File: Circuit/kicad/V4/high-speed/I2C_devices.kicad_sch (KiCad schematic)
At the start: 78 parts, among them U15 LSF0108PWR, U16 TCA9548APWR, U17 LSF0108PWR, U18 TCA9548APWR

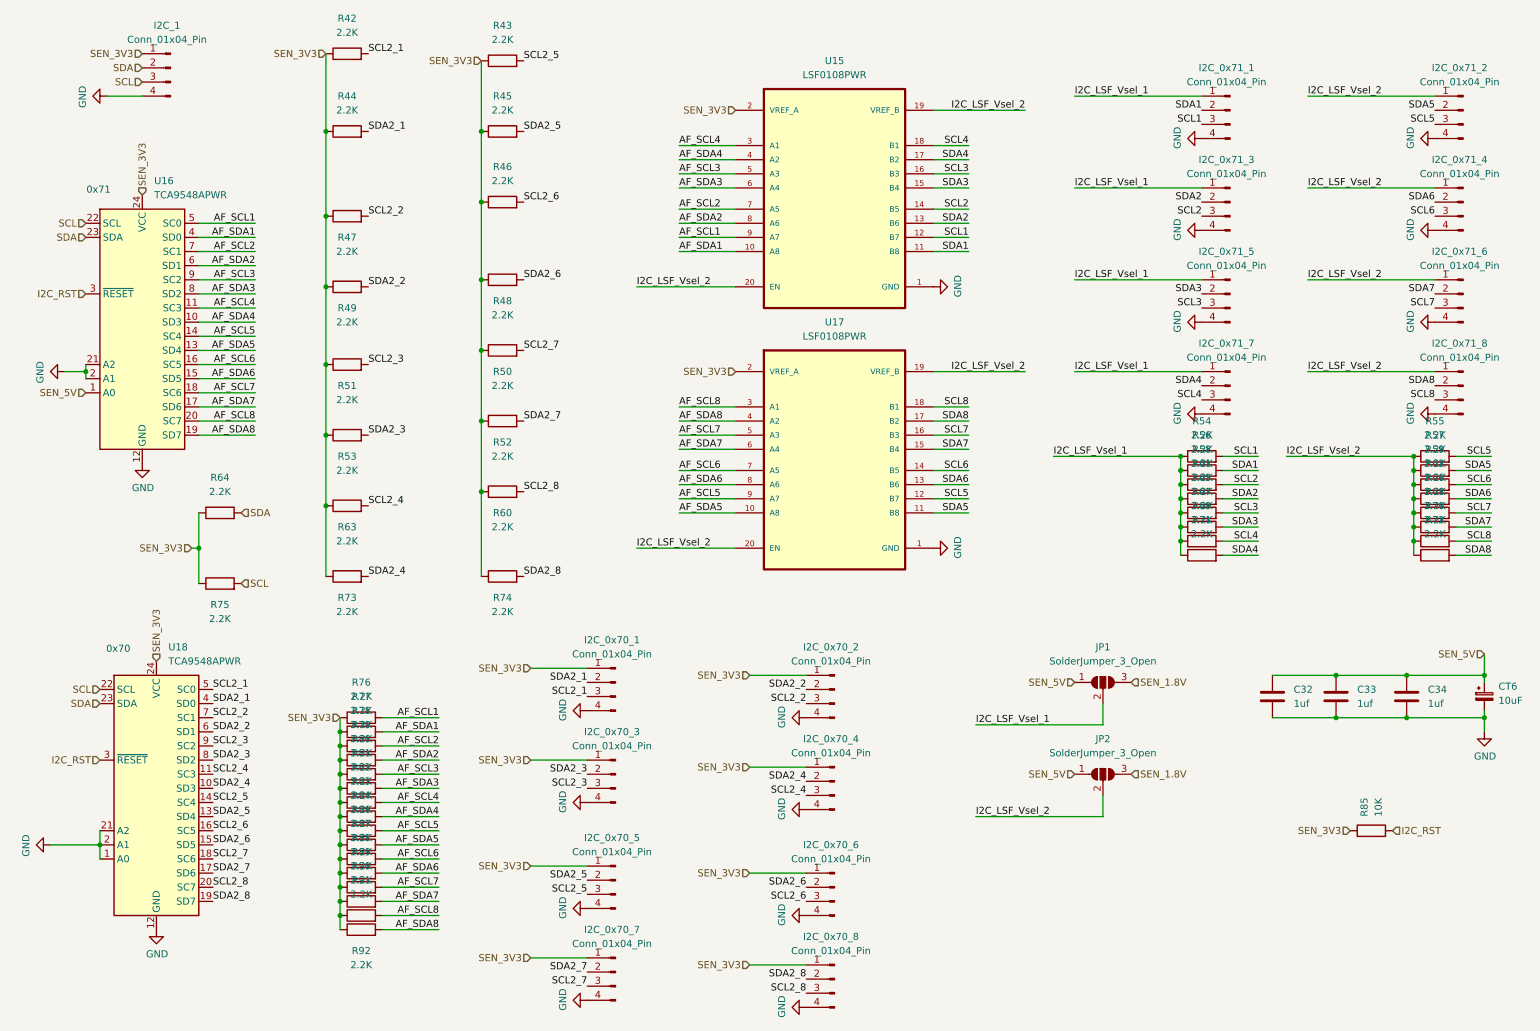
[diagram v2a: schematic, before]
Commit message: finished high-speed panel schematic and first try to doute gpios
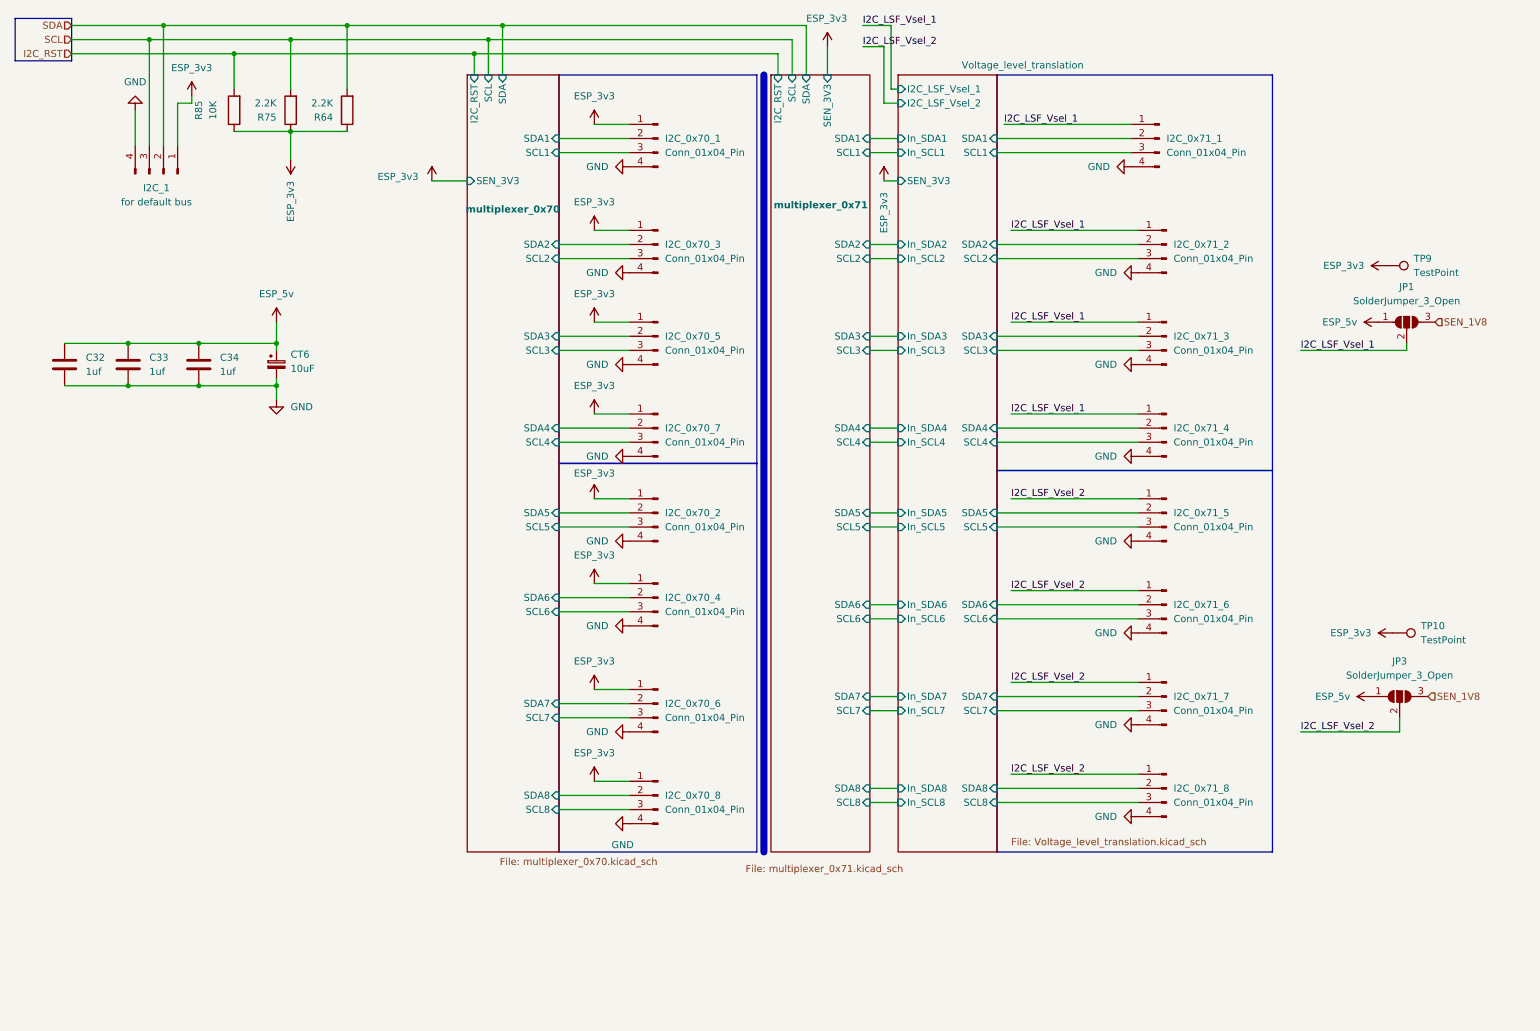
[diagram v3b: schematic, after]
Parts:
- removed JP2: SolderJumper_3_Open, Jumper:SolderJumper-3_P1.3mm_Open_RoundedPad1.0x1.5mm, symbol Jumper:SolderJumper_3_Open
- removed R42, R43, R44, R45, R46, R47, R48, R49, R50, R51, R52, R53, R54, R55, R56, R57, R58, R59, R60, R61, R62, R63, R65, R66, R67, R68, R69, R70, R71, R72, R73, R74, R76, R77, R78, R79, R80, R81, R82, R83, R84, R86, R87, R88, R89, R90, R91, R92: 2.2K, Capacitor_SMD:C_0603_1608Metric, symbol Device:R
- removed U15, U17: LSF0108PWR, panel:SOP65P640X120-20N, symbol LSF0108:LSF0108PWR
- removed U16, U18: TCA9548APWR, Package_SO:TSSOP-24_4.4x7.8mm_P0.65mm, symbol Interface_Expansion:TCA9548APWR
- added JP3: SolderJumper_3_Open, Jumper:SolderJumper-3_P1.3mm_Open_RoundedPad1.0x1.5mm, symbol Jumper:SolderJumper_3_Open
- added TP10, TP9: TestPoint, TestPoint:TestPoint_Pad_D1.0mm, symbol Connector:TestPoint
- CT6: footprint Capacitor_Tantalum_SMD:CP_EIA-3528-21_Kemet-B -> Capacitor_Tantalum_SMD:CP_EIA-3216-18_Kemet-A_HandSolder
- I2C_1: value Conn_01x04_Pin -> for default bus
- renumbered I2C_0x71_3 to I2C_0x71_2, I2C_0x71_5 to I2C_0x71_3, I2C_0x71_7 to I2C_0x71_4, I2C_0x71_2 to I2C_0x71_5, I2C_0x71_4 to I2C_0x71_6, I2C_0x71_6 to I2C_0x71_7
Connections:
- net I2C_LSF_Vsel_2: now also JP3.2 (C)
- net SCL1 renamed Voltage_level_translation/SCL1
- net SCL2 renamed Voltage_level_translation/SCL2
- net SCL2_1 renamed multiplexer_0x70/SCL1
- net SCL2_2 renamed multiplexer_0x70/SCL5
- net SCL2_3 renamed multiplexer_0x70/SCL2
- net SCL2_4 renamed multiplexer_0x70/SCL6
- net SCL2_5 renamed multiplexer_0x70/SCL3
- net SCL2_6 renamed multiplexer_0x70/SCL7
- net SCL2_7 renamed multiplexer_0x70/SCL4
- net SCL2_8 renamed multiplexer_0x70/SCL8
- net SCL3 renamed Voltage_level_translation/SCL3
- net SCL4 renamed Voltage_level_translation/SCL4
- net SCL5 renamed Voltage_level_translation/SCL5
- net SCL6 renamed Voltage_level_translation/SCL6
- net SCL7 renamed Voltage_level_translation/SCL7
- net SCL8 renamed Voltage_level_translation/SCL8
- net SDA1 renamed Voltage_level_translation/SDA1
- net SDA2 renamed Voltage_level_translation/SDA2
- net SDA2_1 renamed multiplexer_0x70/SDA1
- net SDA2_2 renamed multiplexer_0x70/SDA5
- net SDA2_3 renamed multiplexer_0x70/SDA2
- net SDA2_4 renamed multiplexer_0x70/SDA6
- net SDA2_5 renamed multiplexer_0x70/SDA3
- net SDA2_6 renamed multiplexer_0x70/SDA7
- net SDA2_7 renamed multiplexer_0x70/SDA4
- net SDA2_8 renamed multiplexer_0x70/SDA8
- net SDA3 renamed Voltage_level_translation/SDA3
- net SDA4 renamed Voltage_level_translation/SDA4
- net SDA5 renamed Voltage_level_translation/SDA5
- net SDA6 renamed Voltage_level_translation/SDA6
- net SDA7 renamed Voltage_level_translation/SDA7
- net SDA8 renamed Voltage_level_translation/SDA8
- net SEN_1.8V renamed SEN_1V8
- net SEN_1V8: now also JP3.3 (B)
- net SEN_3V3 renamed ESP_3v3
- net ESP_3v3: now also TP10.1, TP9.1
- net SEN_5V renamed ESP_5v
- net ESP_5v: now also JP3.1 (A)
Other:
- added sheet Voltage_level_translation (Voltage_level_translation.kicad_sch)
- added sheet multiplexer_0x70 (multiplexer_0x70.kicad_sch)
- added sheet multiplexer_0x71 (multiplexer_0x71.kicad_sch)
- note removed: "0x70"
- note removed: "0x71"
- moved on the sheet: C32, C33, C34, CT6, I2C_0x70_1, I2C_0x70_2, I2C_0x70_3, I2C_0x70_4, I2C_0x70_5, I2C_0x70_6, I2C_0x70_7, I2C_0x70_8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

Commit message: pcb update
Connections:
- net multiplexer_0x70/SCL2: now also I2C_0x70_2.3 (Pin_3); no longer I2C_0x70_3.3 (Pin_3)
- net multiplexer_0x70/SCL3: now also I2C_0x70_3.3 (Pin_3); no longer I2C_0x70_5.3 (Pin_3)
- net multiplexer_0x70/SCL4: now also I2C_0x70_4.3 (Pin_3); no longer I2C_0x70_7.3 (Pin_3)
- net multiplexer_0x70/SCL5: now also I2C_0x70_5.3 (Pin_3); no longer I2C_0x70_2.3 (Pin_3)
- net multiplexer_0x70/SCL6: now also I2C_0x70_6.3 (Pin_3); no longer I2C_0x70_4.3 (Pin_3)
- net multiplexer_0x70/SCL7: now also I2C_0x70_7.3 (Pin_3); no longer I2C_0x70_6.3 (Pin_3)
- net multiplexer_0x70/SDA2: now also I2C_0x70_2.2 (Pin_2); no longer I2C_0x70_3.2 (Pin_2)
- net multiplexer_0x70/SDA3: now also I2C_0x70_3.2 (Pin_2); no longer I2C_0x70_5.2 (Pin_2)
- net multiplexer_0x70/SDA4: now also I2C_0x70_4.2 (Pin_2); no longer I2C_0x70_7.2 (Pin_2)
- net multiplexer_0x70/SDA5: now also I2C_0x70_5.2 (Pin_2); no longer I2C_0x70_2.2 (Pin_2)
- net multiplexer_0x70/SDA6: now also I2C_0x70_6.2 (Pin_2); no longer I2C_0x70_4.2 (Pin_2)
- net multiplexer_0x70/SDA7: now also I2C_0x70_7.2 (Pin_2); no longer I2C_0x70_6.2 (Pin_2)
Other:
- moved on the sheet: I2C_0x70_2, I2C_0x70_3, I2C_0x70_4, I2C_0x70_5, I2C_0x70_6, I2C_0x70_7
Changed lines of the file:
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@@
 	(symbol
 		(lib_id "Connector:Conn_01x04_Pin")
-		(at 128.27 54.61 0)
+		(at 128.27 71.12 0)
 		(mirror y)
 		(unit 1)
@@
 		(fields_autoplaced yes)
 		(property "Reference" "I2C_0x70_3"
-			(at 129.54 54.6099 0)
+			(at 129.54 71.1199 0)
 			(effects
 				(font
@@
 		)
 		(property "Value" "Conn_01x04_Pin"
-			(at 129.54 57.1499 0)
+			(at 129.54 73.6599 0)
 			(effects
 				(font
@@
 		)
 		(property "Footprint" "Connector_JST:JST_SH_BM04B-SRSS-TB_1x04-1MP_P1.00mm_Vertical"
-			(at 128.27 54.61 0)
+			(at 128.27 71.12 0)
 			(effects
 				(font
@@
 		)
 		(property "Datasheet" "https://www.hestore.hu/prod_getfile.php?id=20105"
-			(at 128.27 54.61 0)
+			(at 128.27 71.12 0)
 			(effects
 				(font
@@
 		)
 		(property "Description" "Generic connector, single row, 01x04, script generated"
-			(at 128.27 54.61 0)
+			(at 128.27 71.12 0)
 			(effects
 				(font
@@
 		)
 		(property "Cikkszám" "100.491.15"
-			(at 128.27 54.61 0)
+			(at 128.27 71.12 0)
 			(effects
 				(font
@@
 		)
 		(property "Link" "https://www.hestore.hu/prod_10049115.html"
-			(at 128.27 54.61 0)
+			(at 128.27 71.12 0)
 			(effects
 				(font
@@
 	(symbol
 		(lib_id "Connector:Conn_01x04_Pin")
-		(at 128.27 118.11 0)
+		(at 128.27 87.63 0)
 		(mirror y)
 		(unit 1)
@@
 		(fields_autoplaced yes)
 		(property "Reference" "I2C_0x70_4"
-			(at 129.54 118.1099 0)
+			(at 129.54 87.6299 0)
 			(effects
 				(font
@@
 		)
 		(property "Value" "Conn_01x04_Pin"
-			(at 129.54 120.6499 0)
+			(at 129.54 90.1699 0)
 			(effects
 				(font
@@
 		)
 		(property "Footprint" "Connector_JST:JST_SH_BM04B-SRSS-TB_1x04-1MP_P1.00mm_Vertical"
-			(at 128.27 118.11 0)
+			(at 128.27 87.63 0)
 			(effects
 				(font
@@
 		)
 		(property "Datasheet" "https://www.hestore.hu/prod_getfile.php?id=20105"
-			(at 128.27 118.11 0)
+			(at 128.27 87.63 0)
 			(effects
 				(font
@@
 		)
 		(property "Description" "Generic connector, single row, 01x04, script generated"
-			(at 128.27 118.11 0)
+			(at 128.27 87.63 0)
 			(effects
 				(font
@@
 		)
 		(property "Cikkszám" "100.491.15"
-			(at 128.27 118.11 0)
+			(at 128.27 87.63 0)
 			(effects
 				(font
@@
 		)
 		(property "Link" "https://www.hestore.hu/prod_10049115.html"
-			(at 128.27 118.11 0)
+			(at 128.27 87.63 0)
 			(effects
 				(font
@@
 	(symbol
 		(lib_id "Connector:Conn_01x04_Pin")
-		(at 128.27 87.63 0)
+		(at 128.27 137.16 0)
 		(mirror y)
 		(unit 1)
@@
 		(fields_autoplaced yes)
 		(property "Reference" "I2C_0x70_7"
-			(at 129.54 87.6299 0)
+			(at 129.54 137.1599 0)
 			(effects
 				(font
@@
 		)
 		(property "Value" "Conn_01x04_Pin"
-			(at 129.54 90.1699 0)
+			(at 129.54 139.6999 0)
 			(effects
 				(font
@@
 		)
 		(property "Footprint" "Connector_JST:JST_SH_BM04B-SRSS-TB_1x04-1MP_P1.00mm_Vertical"
-			(at 128.27 87.63 0)
+			(at 128.27 137.16 0)
 			(effects
 				(font
@@
 		)
 		(property "Datasheet" "https://www.hestore.hu/prod_getfile.php?id=20105"
-			(at 128.27 87.63 0)
+			(at 128.27 137.16 0)
 			(effects
 				(font
@@
 		)
 		(property "Description" "Generic connector, single row, 01x04, script generated"
-			(at 128.27 87.63 0)
+			(at 128.27 137.16 0)
 			(effects
 				(font
@@
 		)
 		(property "Cikkszám" "100.491.15"
-			(at 128.27 87.63 0)
+			(at 128.27 137.16 0)
 			(effects
 				(font
@@
 		)
 		(property "Link" "https://www.hestore.hu/prod_10049115.html"
-			(at 128.27 87.63 0)
+			(at 128.27 137.16 0)
 			(effects
 				(font
@@
 	(symbol
 		(lib_id "Connector:Conn_01x04_Pin")
-		(at 128.27 102.87 0)
+		(at 128.27 54.61 0)
 		(mirror y)
 		(unit 1)
@@
 		(fields_autoplaced yes)
 		(property "Reference" "I2C_0x70_2"
-			(at 129.54 102.8699 0)
+			(at 129.54 54.6099 0)
 			(effects
 				(font
@@
 		)
 		(property "Value" "Conn_01x04_Pin"
-			(at 129.54 105.4099 0)
+			(at 129.54 57.1499 0)
 			(effects
 				(font
@@
 		)
 		(property "Footprint" "Connector_JST:JST_SH_BM04B-SRSS-TB_1x04-1MP_P1.00mm_Vertical"
-			(at 128.27 102.87 0)
+			(at 128.27 54.61 0)
 			(effects
 				(font
@@
 		)
 		(property "Datasheet" "https://www.hestore.hu/prod_getfile.php?id=20105"
-			(at 128.27 102.87 0)
+			(at 128.27 54.61 0)
 			(effects
 				(font
@@
 		)
 		(property "Description" "Generic connector, single row, 01x04, script generated"
-			(at 128.27 102.87 0)
+			(at 128.27 54.61 0)
 			(effects
 				(font
@@
 		)
 		(property "Cikkszám" "100.491.15"
-			(at 128.27 102.87 0)
+			(at 128.27 54.61 0)
 			(effects
 				(font
@@
 		)
 		(property "Link" "https://www.hestore.hu/prod_10049115.html"
-			(at 128.27 102.87 0)
+			(at 128.27 54.61 0)
 			(effects
 				(font
@@
 	(symbol
 		(lib_id "Connector:Conn_01x04_Pin")
-		(at 128.27 71.12 0)
+		(at 128.27 102.87 0)
 		(mirror y)
 		(unit 1)
@@
 		(fields_autoplaced yes)
 		(property "Reference" "I2C_0x70_5"
-			(at 129.54 71.1199 0)
+			(at 129.54 102.8699 0)
 			(effects
 				(font
@@
 		)
 		(property "Value" "Conn_01x04_Pin"
-			(at 129.54 73.6599 0)
+			(at 129.54 105.4099 0)
 			(effects
 				(font
@@
 		)
 		(property "Footprint" "Connector_JST:JST_SH_BM04B-SRSS-TB_1x04-1MP_P1.00mm_Vertical"
-			(at 128.27 71.12 0)
+			(at 128.27 102.87 0)
 			(effects
 				(font
@@
 		)
 		(property "Datasheet" "https://www.hestore.hu/prod_getfile.php?id=20105"
-			(at 128.27 71.12 0)
+			(at 128.27 102.87 0)
 			(effects
 				(font
@@
 		)
 		(property "Description" "Generic connector, single row, 01x04, script generated"
-			(at 128.27 71.12 0)
+			(at 128.27 102.87 0)
 			(effects
 				(font
@@
 		)
 		(property "Cikkszám" "100.491.15"
-			(at 128.27 71.12 0)
+			(at 128.27 102.87 0)
 			(effects
 				(font
@@
 		)
 		(property "Link" "https://www.hestore.hu/prod_10049115.html"
-			(at 128.27 71.12 0)
+			(at 128.27 102.87 0)
 			(effects
 				(font
@@
 	(symbol
 		(lib_id "Connector:Conn_01x04_Pin")
-		(at 128.27 137.16 0)
+		(at 128.27 118.11 0)
 		(mirror y)
 		(unit 1)
@@
 		(on_board yes)
 		(dnp no)
-		(fields_autoplaced yes)
 		(property "Reference" "I2C_0x70_6"
-			(at 129.54 137.1599 0)
+			(at 129.54 118.1099 0)
 			(effects
 				(font
@@
 		)
 		(property "Value" "Conn_01x04_Pin"
-			(at 129.54 139.6999 0)
+			(at 129.54 120.6499 0)
 			(effects
 				(font
@@
 		)
 		(property "Footprint" "Connector_JST:JST_SH_BM04B-SRSS-TB_1x04-1MP_P1.00mm_Vertical"
-			(at 128.27 137.16 0)
+			(at 128.27 118.11 0)
 			(effects
 				(font
@@
 		)
 		(property "Datasheet" "https://www.hestore.hu/prod_getfile.php?id=20105"
-			(at 128.27 137.16 0)
+			(at 128.27 118.11 0)
 			(effects
 				(font
@@
 		)
 		(property "Description" "Generic connector, single row, 01x04, script generated"
-			(at 128.27 137.16 0)
+			(at 128.27 118.11 0)
 			(effects
 				(font
@@
 		)
 		(property "Cikkszám" "100.491.15"
-			(at 128.27 137.16 0)
+			(at 128.27 118.11 0)
 			(effects
 				(font
@@
 		)
 		(property "Link" "https://www.hestore.hu/prod_10049115.html"
-			(at 128.27 137.16 0)
+			(at 128.27 118.11 0)
 			(effects
 				(font
